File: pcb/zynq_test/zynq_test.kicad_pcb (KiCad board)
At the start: 2 copper layers, 100 x 100 mm, 19 parts, among them J1002 USB_A, J1101 RJ45_JK0654219, J1201 1-1734248-5, J1202 1-1734248-5, J1204 1-1734248-5, J702 USB_B_Micro, J801 HDMI_A, J802 HDMI_A, J901 A-MicroTF-1.85A, U1002 TUSB1210-Q1, U1003 AP22816AKBWT, U1102 LAN8830, U202 XC7Z020-2CLG400I, U401 MT41K256M16TW-107, U402 MT41K256M16TW-107, U702 FT2232HQ, U803 TDP1204RNQR, U806 TDP1204RNQR, U901 TXS02612RTW

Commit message: Finished Power Supply
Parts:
- moved J1204 23.1 mm to (175.0, 76.0), turned to 90 degrees
- moved J1201 20.3 mm to (152.0, 122.5), turned to -90 degrees
- moved J1002 16.4 mm to (124.5, 47.0)
- moved U1002 15.9 mm to (125.2, 61.5)
- moved J1202 14.2 mm to (159.7, 122.5), turned to 90 degrees
- moved U702 9.55 mm to (162.8, 61.5)
- moved J801 7.40 mm to (175.5, 118.7)
- moved J802 7.40 mm to (175.1, 99.2)
- moved U803 7.40 mm to (160.9, 97.2)
- moved U806 7.40 mm to (161.1, 117.6)
- moved U901 5.92 mm to (138.6, 68.8)
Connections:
- J1101 pad 14: +3.3V -> +3V3
- J1101 pad 16: +3.3V -> +3V3
- J1201 pad 10: unconnected-(J1201-Pad10) -> GND
- J1201 pad 10_1: unconnected-(J1201-10__1-Pad10_1) -> GND
- J1201 pad 11: unconnected-(J1201-Pad11) -> /Cameras/CAM0.GPIO0
- J1201 pad 11_1: unconnected-(J1201-11__1-Pad11_1) -> /Cameras/CAM0.GPIO0
- J1201 pad 12: unconnected-(J1201-Pad12) -> /Cameras/CAM0.GPIO1
- J1201 pad 12_1: unconnected-(J1201-12__1-Pad12_1) -> /Cameras/CAM0.GPIO1
- J1201 pad 13: unconnected-(J1201-Pad13) -> /Cameras/CAM_RX.0.I2C_CLK
- J1201 pad 13_1: unconnected-(J1201-13__1-Pad13_1) -> /Cameras/CAM_RX.0.I2C_CLK
- J1201 pad 14: unconnected-(J1201-Pad14) -> /Cameras/CAM_RX.0.I2C_SDA
- J1201 pad 14_1: unconnected-(J1201-14__1-Pad14_1) -> /Cameras/CAM_RX.0.I2C_SDA
- J1201 pad 15: unconnected-(J1201-Pad15) -> +3V3
- J1201 pad 15_1: unconnected-(J1201-15__1-Pad15_1) -> +3V3
- J1201 pad 1_1: /Cameras/CAM_RX.0.CAM_D0_N -> GND
- J1201 pad 2: /Cameras/CAM_RX.0.CAM_D0_P -> /Cameras/CAM_RX.0.CAM_D0_N
- J1201 pad 2_1: GND -> /Cameras/CAM_RX.0.CAM_D0_N
- J1201 pad 3: /Cameras/CAM_RX.0.CAM_D1_N -> /Cameras/CAM_RX.0.CAM_D0_P
- J1201 pad 3_1: /Cameras/CAM_RX.0.CAM_D1_P -> /Cameras/CAM_RX.0.CAM_D0_P
- J1201 pad 4_1: /Cameras/CAM_RX.0.CAM_CLK_N -> GND
- J1201 pad 5: /Cameras/CAM_RX.0.CAM_CLK_P -> /Cameras/CAM_RX.0.CAM_D1_N
- J1201 pad 5_1: GND -> /Cameras/CAM_RX.0.CAM_D1_N
- J1201 pad 6: /Cameras/CAM0.GPIO0 -> /Cameras/CAM_RX.0.CAM_D1_P
- J1201 pad 6_1: /Cameras/CAM0.GPIO1 -> /Cameras/CAM_RX.0.CAM_D1_P
- J1201 pad 7: /Cameras/CAM_RX.0.I2C_CLK -> GND
- J1201 pad 7_1: /Cameras/CAM_RX.0.I2C_SDA -> GND
- J1201 pad 8: +3.3V -> /Cameras/CAM_RX.0.CAM_CLK_N
- J1201 pad 8_1: unconnected-(J1201-8__1-Pad8_1) -> /Cameras/CAM_RX.0.CAM_CLK_N
- J1201 pad 9: unconnected-(J1201-Pad9) -> /Cameras/CAM_RX.0.CAM_CLK_P
- J1201 pad 9_1: unconnected-(J1201-9__1-Pad9_1) -> /Cameras/CAM_RX.0.CAM_CLK_P
- J1202 pad 10: unconnected-(J1202-Pad10) -> GND
- J1202 pad 10_1: unconnected-(J1202-10__1-Pad10_1) -> GND
- J1202 pad 11: unconnected-(J1202-Pad11) -> /Cameras/CAM1.GPIO0
- J1202 pad 11_1: unconnected-(J1202-11__1-Pad11_1) -> /Cameras/CAM1.GPIO0
- J1202 pad 12: unconnected-(J1202-Pad12) -> /Cameras/CAM1.GPIO1
- J1202 pad 12_1: unconnected-(J1202-12__1-Pad12_1) -> /Cameras/CAM1.GPIO1
- J1202 pad 13: unconnected-(J1202-Pad13) -> /Cameras/CAM_RX.1.I2C_CLK
- J1202 pad 13_1: unconnected-(J1202-13__1-Pad13_1) -> /Cameras/CAM_RX.1.I2C_CLK
- J1202 pad 14: unconnected-(J1202-Pad14) -> /Cameras/CAM_RX.1.I2C_SDA
- J1202 pad 14_1: unconnected-(J1202-14__1-Pad14_1) -> /Cameras/CAM_RX.1.I2C_SDA
- J1202 pad 15: unconnected-(J1202-Pad15) -> +3V3
- J1202 pad 15_1: unconnected-(J1202-15__1-Pad15_1) -> +3V3
- J1202 pad 1_1: /Cameras/CAM_RX.1.CAM_D0_N -> GND
- J1202 pad 2: /Cameras/CAM_RX.1.CAM_D0_P -> /Cameras/CAM_RX.1.CAM_D0_N
- J1202 pad 2_1: GND -> /Cameras/CAM_RX.1.CAM_D0_N
- J1202 pad 3: /Cameras/CAM_RX.1.CAM_D1_N -> /Cameras/CAM_RX.1.CAM_D0_P
- J1202 pad 3_1: /Cameras/CAM_RX.1.CAM_D1_P -> /Cameras/CAM_RX.1.CAM_D0_P
- J1202 pad 4_1: /Cameras/CAM_RX.1.CAM_CLK_N -> GND
- J1202 pad 5: /Cameras/CAM_RX.1.CAM_CLK_P -> /Cameras/CAM_RX.1.CAM_D1_N
- J1202 pad 5_1: GND -> /Cameras/CAM_RX.1.CAM_D1_N
- J1202 pad 6: /Cameras/CAM1.GPIO0 -> /Cameras/CAM_RX.1.CAM_D1_P
- J1202 pad 6_1: /Cameras/CAM1.GPIO1 -> /Cameras/CAM_RX.1.CAM_D1_P
- J1202 pad 7: /Cameras/CAM_RX.1.I2C_CLK -> GND
- J1202 pad 7_1: /Cameras/CAM_RX.1.I2C_SDA -> GND
- J1202 pad 8: +3.3V -> /Cameras/CAM_RX.1.CAM_CLK_N
- J1202 pad 8_1: unconnected-(J1202-8__1-Pad8_1) -> /Cameras/CAM_RX.1.CAM_CLK_N
- J1202 pad 9: unconnected-(J1202-Pad9) -> /Cameras/CAM_RX.1.CAM_CLK_P
- J1202 pad 9_1: unconnected-(J1202-9__1-Pad9_1) -> /Cameras/CAM_RX.1.CAM_CLK_P
- J1204 pad 10: unconnected-(J1204-Pad10) -> GND
- J1204 pad 10_1: unconnected-(J1204-10__1-Pad10_1) -> GND
- J1204 pad 11: unconnected-(J1204-Pad11) -> /Cameras/CAM2.GPIO0
- J1204 pad 11_1: unconnected-(J1204-11__1-Pad11_1) -> /Cameras/CAM2.GPIO0
- J1204 pad 12: unconnected-(J1204-Pad12) -> /Cameras/CAM2.GPIO1
- J1204 pad 12_1: unconnected-(J1204-12__1-Pad12_1) -> /Cameras/CAM2.GPIO1
- J1204 pad 13: unconnected-(J1204-Pad13) -> /Cameras/CAM_TX.2.I2C_CLK
- J1204 pad 13_1: unconnected-(J1204-13__1-Pad13_1) -> /Cameras/CAM_TX.2.I2C_CLK
- J1204 pad 14: unconnected-(J1204-Pad14) -> /Cameras/CAM_TX.2.I2C_SDA
- J1204 pad 14_1: unconnected-(J1204-14__1-Pad14_1) -> /Cameras/CAM_TX.2.I2C_SDA
- J1204 pad 15: unconnected-(J1204-Pad15) -> +3V3
- J1204 pad 15_1: unconnected-(J1204-15__1-Pad15_1) -> +3V3
- J1204 pad 1_1: /Cameras/CAM2.TX.0_N -> GND
- J1204 pad 2: /Cameras/CAM2.TX.0_P -> /Cameras/CAM2.TX.0_N
- J1204 pad 2_1: GND -> /Cameras/CAM2.TX.0_N
- J1204 pad 3: /Cameras/CAM2.TX.1_N -> /Cameras/CAM2.TX.0_P
- J1204 pad 3_1: /Cameras/CAM2.TX.1_P -> /Cameras/CAM2.TX.0_P
- J1204 pad 4_1: /Cameras/CAM2.TX.CLK_N -> GND
- J1204 pad 5: /Cameras/CAM2.TX.CLK_P -> /Cameras/CAM2.TX.1_N
- J1204 pad 5_1: GND -> /Cameras/CAM2.TX.1_N
- J1204 pad 6: /Cameras/CAM2.GPIO0 -> /Cameras/CAM2.TX.1_P
- J1204 pad 6_1: /Cameras/CAM2.GPIO1 -> /Cameras/CAM2.TX.1_P
- J1204 pad 7: /Cameras/CAM_TX.2.I2C_CLK -> GND
- J1204 pad 7_1: /Cameras/CAM_TX.2.I2C_SDA -> GND
- J1204 pad 8: +3.3V -> /Cameras/CAM2.TX.CLK_N
- J1204 pad 8_1: unconnected-(J1204-8__1-Pad8_1) -> /Cameras/CAM2.TX.CLK_N
- J1204 pad 9: unconnected-(J1204-Pad9) -> /Cameras/CAM2.TX.CLK_P
- J1204 pad 9_1: unconnected-(J1204-9__1-Pad9_1) -> /Cameras/CAM2.TX.CLK_P
- J901 pad 4: +3.3V -> +3V3
- U1002 pad 20: +3.3V -> +3V3
- U1002 pad 21: +3.3V -> +3V3
- U1003 pad 3: unconnected-(U1003-~{FLG}-Pad3) -> +5V
- U1003 pad 5: +5V -> +5V_{USB_OTG}
- U202 pad B6: +3.3V -> +3V3
- U202 pad C19: Net-(C302-Pad1) -> +3V3
- U202 pad D7: +3.3V -> +3V3
- U202 pad F18: Net-(C302-Pad1) -> +3V3
- U202 pad H14: Net-(C302-Pad1) -> +3V3
- U202 pad J17: Net-(C302-Pad1) -> +3V3
- U202 pad K20: Net-(C302-Pad1) -> +3V3
- U202 pad K6: +3.3V -> +3V3
- U202 pad M16: Net-(C302-Pad1) -> +3V3
- U202 pad M6: +3.3V -> +3V3
- U202 pad N19: Net-(C315-Pad1) -> +3V3
- U202 pad N6: +3.3V -> +3V3
- U202 pad R15: Net-(C315-Pad1) -> +3V3
- U202 pad R6: +3.3V -> +3V3
- U202 pad T18: Net-(C315-Pad1) -> +3V3
- U202 pad T6: +3.3V -> +3V3
- U202 pad T8: Net-(C301-Pad1) -> +3V3
- U202 pad U11: Net-(C301-Pad1) -> +3V3
- U202 pad V14: Net-(C315-Pad1) -> +3V3
- U202 pad W17: Net-(C315-Pad1) -> +3V3
- U202 pad W7: Net-(C301-Pad1) -> +3V3
- U202 pad Y10: Net-(C301-Pad1) -> +3V3
- U202 pad Y20: Net-(C315-Pad1) -> +3V3
- U702 pad 20: +3.3V -> +3V3
- U702 pad 31: +3.3V -> +3V3
- U702 pad 42: +3.3V -> +3V3
- U702 pad 50: +3.3V -> +3V3
- U702 pad 56: +3.3V -> +3V3
- U803 pad 1: +3.3V -> +3V3
- U803 pad 14: +3.3V -> +3V3
- U803 pad 20: +3.3V -> +3V3
- U803 pad 28: +3.3V -> +3V3
- U803 pad 6: +3.3V -> +3V3
- U803 pad 7: /HDMI/TX_EQ0 -> /HDMI/HDMI.EN
- U806 pad 1: +3.3V -> +3V3
- U806 pad 10: /HDMI/HDMI.RX.D2_N -> Net-(J801-D2-)
- U806 pad 11: Net-(J801-HPD) -> unconnected-(U806-HPD_OUT-Pad11)
- U806 pad 12: /HDMI/HDMI.RX.D1_P -> Net-(J801-D1+)
- U806 pad 13: /HDMI/HDMI.RX.D1_N -> Net-(J801-D1-)
- U806 pad 14: +3.3V -> +3V3
- U806 pad 15: /HDMI/HDMI.RX.D0_P -> Net-(J801-D0+)
- U806 pad 16: /HDMI/HDMI.RX.D0_N -> Net-(J801-D0-)
- U806 pad 18: /HDMI/HDMI.RX.CLK_P -> Net-(J801-CK+)
- U806 pad 19: /HDMI/HDMI.RX.CLK_N -> Net-(J801-CK-)
- U806 pad 20: +3.3V -> +3V3
- U806 pad 28: +3.3V -> +3V3
- U806 pad 30: Net-(J801-CK-) -> /HDMI/HDMI.RX.CLK_N
- U806 pad 31: Net-(J801-CK+) -> /HDMI/HDMI.RX.CLK_P
- U806 pad 32: unconnected-(U806-HPD_IN-Pad32) -> Net-(J801-HPD)
- U806 pad 33: Net-(J801-D0-) -> /HDMI/HDMI.RX.D0_N
- U806 pad 34: Net-(J801-D0+) -> /HDMI/HDMI.RX.D0_P
- U806 pad 36: Net-(J801-D1-) -> /HDMI/HDMI.RX.D1_N
- U806 pad 37: Net-(J801-D1+) -> /HDMI/HDMI.RX.D1_P
- U806 pad 39: Net-(J801-D2-) -> /HDMI/HDMI.RX.D2_N
- U806 pad 40: Net-(J801-D2+) -> /HDMI/HDMI.RX.D2_P
- U806 pad 6: +3.3V -> +3V3
- U806 pad 7: /HDMI/RX_EQ0 -> /HDMI/HDMI.EN
- U806 pad 9: /HDMI/HDMI.RX.D2_P -> Net-(J801-D2+)
- U901 pad 17: +3.3V -> +3V3
- U901 pad 21: +3.3V -> +3V3
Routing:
- net /USB_OTG/USB_OTG.D-: track 0.00 -> 0.88 mm

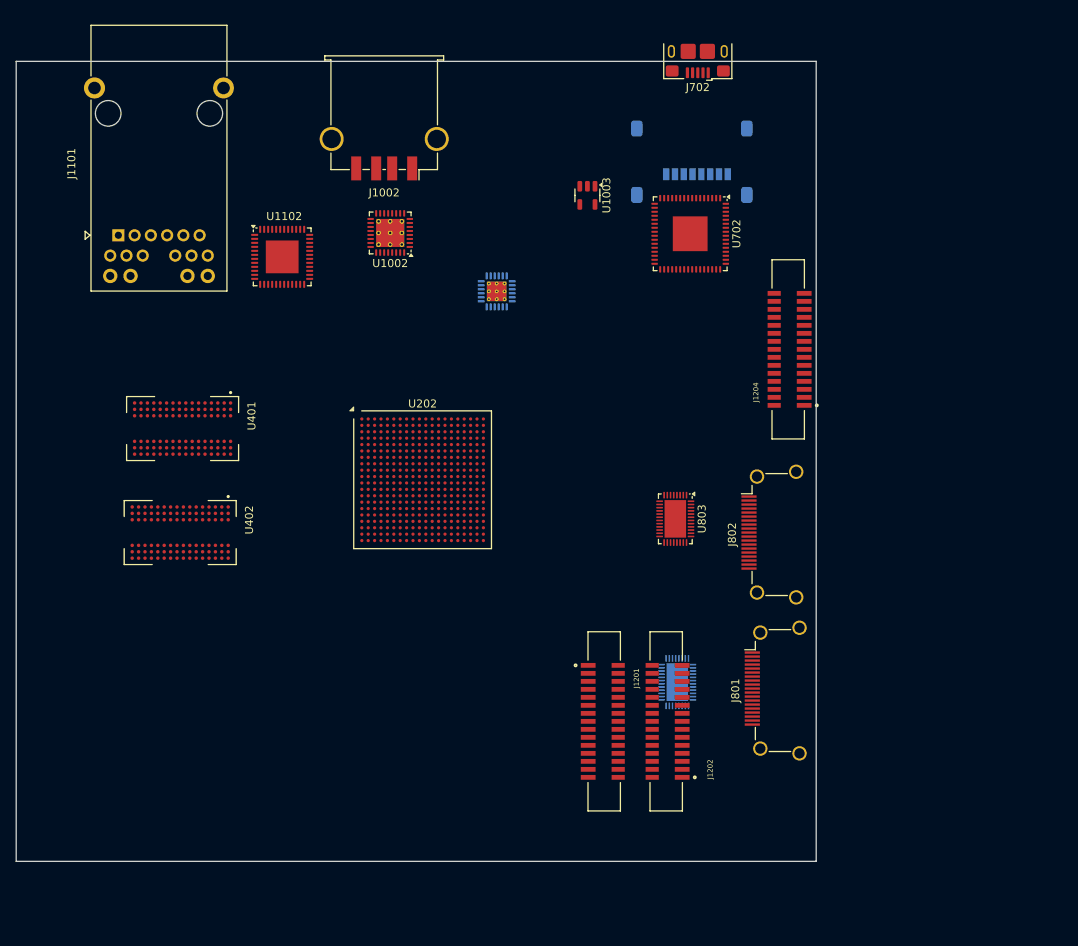
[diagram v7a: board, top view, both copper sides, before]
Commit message: Finished most of the schematic, will start routing soon
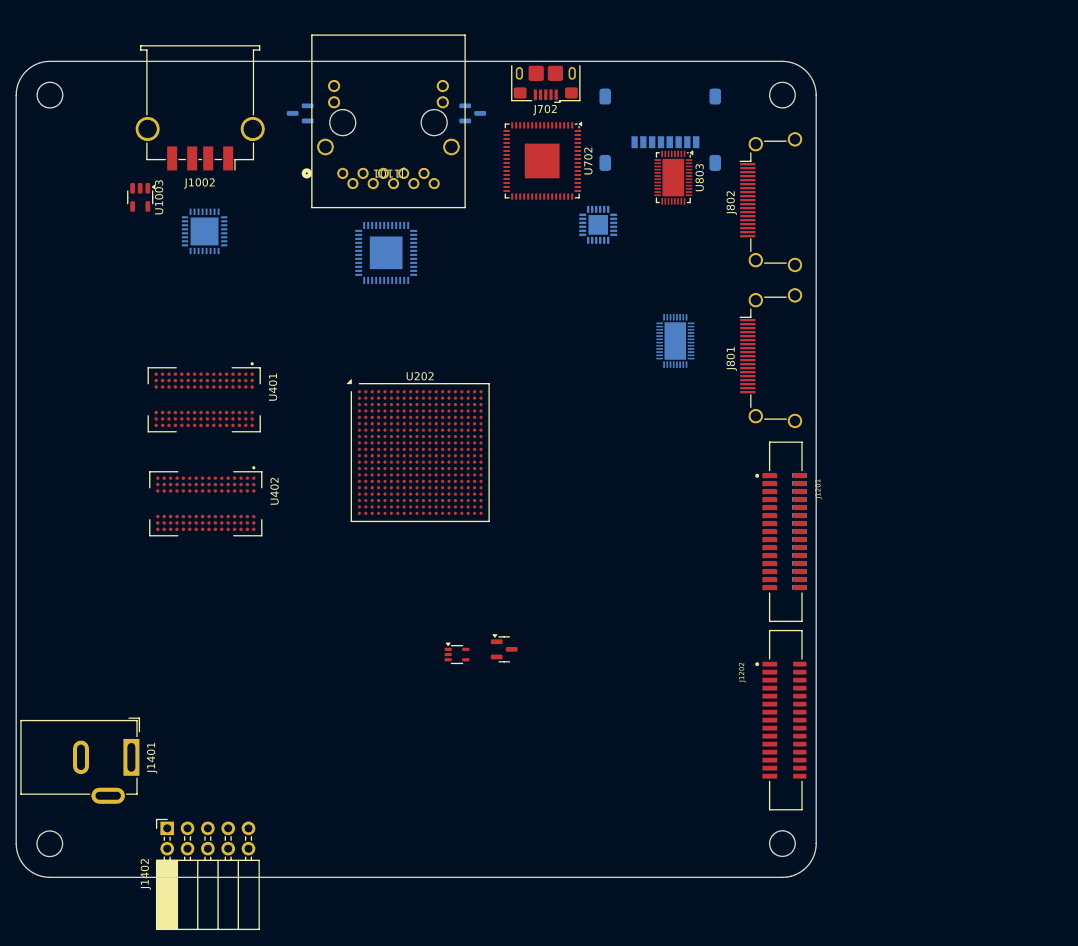
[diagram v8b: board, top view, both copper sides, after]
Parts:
- added J1401: Barrel_Jack, Connector_BarrelJack:BarrelJack_GCT_DCJ200-10-A_Horizontal, F.Cu at (92.9, 127.0)
- added J1402: Conn_02x05_Odd_Even, Connector_PinSocket_2.54mm:PinSocket_2x05_P2.54mm_Horizontal, F.Cu at (97.4, 135.9)
- added Q1102: 2N7002E, Package_TO_SOT_SMD:SOT-23, B.Cu at (135.6, 46.5)
- added Q1103: 2N7002E, Package_TO_SOT_SMD:SOT-23, B.Cu at (114.0, 46.5)
- added Q1104: 2N7002E, Package_TO_SOT_SMD:SOT-23, F.Cu at (139.5, 113.5)
- added U1405: 74LVC1G17, Package_TO_SOT_SMD:Texas_R-PDSO-G5_DCK-5, F.Cu at (133.6, 114.2)
- J1101: footprint Connector_RJ:RJ45_Pulse_JK0654219NL_Horizontal -> ethernet:ARJM11C7-502-AB-ER2-T_ABR
- J1204, U1102: moved to B.Cu
- U1002: footprint Package_DFN_QFN:VQFN-32-1EP_5x5mm_P0.5mm_EP3.5x3.5mm_ThermalVias -> Package_DFN_QFN:VQFN-32-1EP_5x5mm_P0.5mm_EP3.5x3.5mm; moved to B.Cu
- U901: footprint Package_DFN_QFN:WQFN-24-1EP_4x4mm_P0.5mm_EP2.45x2.45mm_ThermalVias -> Package_DFN_QFN:WQFN-24-1EP_4x4mm_P0.5mm_EP2.45x2.45mm
- moved U1003 55.9 mm to (94.0, 57.0)
- moved U803 42.7 mm to (160.6, 54.5)
- moved U806 42.7 mm to (160.9, 75.0)
- moved J801 41.6 mm to (174.9, 77.1)
- moved J802 41.6 mm to (174.9, 57.6)
- moved J1201 32.8 mm to (174.7, 98.8)
- moved J1101 29.1 mm to (119.3, 54.0), turned to 180 degrees
- moved U1002 23.2 mm to (102.0, 61.2), turned to 90 degrees
- moved J1002 23.0 mm to (101.5, 45.8)
- moved J1204 22.8 mm to (174.4, 98.8), turned to -90 degrees
- moved U702 20.6 mm to (144.2, 52.5)
- moved J702 19.2 mm to (144.7, 41.5)
- moved U901 15.2 mm to (151.2, 60.4)
- moved J1202 15.0 mm to (174.7, 122.3), turned to -90 degrees
- moved U1102 13.0 mm to (124.8, 63.9), turned to -90 degrees
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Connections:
- net /Zynq Mio/MIO0.0 renamed /GPIO/MIO0.0
- net /Zynq Mio/MIO0.10 renamed /GPIO/MIO0.10
- net /Zynq Mio/MIO0.11 renamed /GPIO/MIO0.11
- net /Zynq Mio/MIO0.12 renamed /GPIO/MIO0.12
- net /Zynq Mio/MIO0.13 renamed /GPIO/MIO0.13
- net /Zynq Mio/MIO0.7 renamed /GPIO/MIO0.7
- net /Zynq Mio/MIO0.8 renamed /GPIO/MIO0.8
- net /Zynq Mio/MIO0.9 renamed /GPIO/MIO0.9
- net /Zynq Mio/MIO1.46 renamed /GPIO/MIO1.46
- net /Zynq Mio/MIO1.47 renamed /GPIO/MIO1.47
- net /Zynq Mio/MIO1.48 renamed /GPIO/MIO1.48
- net /Zynq Mio/MIO1.49 renamed /GPIO/MIO1.49
- net /Zynq Mio/MIO1.50 renamed /GPIO/MIO1.50
- net /Zynq Mio/MIO1.51 renamed /GPIO/MIO1.51
- J1101 pad 1: /ETHERNET/ETH_TX3_C -> /ETHERNET/ETH_TX1_P
- J1101 pad 10: /ETHERNET/ETH_TX1_N -> /ETHERNET/ETH_TX4_N
- J1101 pad 11: /ETHERNET/ETH_TX1_P -> +3V3
- J1101 pad 12: /ETHERNET/ETH_TX1_C -> /ETHERNET/LED1
- J1101 pad 13: /ETHERNET/LED2 -> +3V3
- J1101 pad 14: +3V3 -> /ETHERNET/LED2
- J1101 pad 2: /ETHERNET/ETH_TX3_N -> /ETHERNET/ETH_TX1_N
- J1101 pad 3: /ETHERNET/ETH_TX3_P -> /ETHERNET/ETH_TX2_P
- J1101 pad 4: /ETHERNET/ETH_TX2_P -> /ETHERNET/ETH_TX2_N
- J1101 pad 5: /ETHERNET/ETH_TX2_N -> Net-(J1101-TRCT1)
- J1101 pad 6: /ETHERNET/ETH_TX2_C -> Net-(J1101-TRCT1)
- J1101 pad 7: /ETHERNET/ETH_TX4_C -> /ETHERNET/ETH_TX3_P
- J1101 pad 8: /ETHERNET/ETH_TX4_P -> /ETHERNET/ETH_TX3_N
- J1101 pad 9: /ETHERNET/ETH_TX4_N -> /ETHERNET/ETH_TX4_P
- J1201 pad 11: /Cameras/CAM0.GPIO0 -> /Cameras/CAM0.GPIO1.
- J1201 pad 11_1: /Cameras/CAM0.GPIO0 -> /Cameras/CAM0.GPIO1.
- J1201 pad 12: /Cameras/CAM0.GPIO1 -> /Cameras/CAM0.GPIO1.
- J1201 pad 12_1: /Cameras/CAM0.GPIO1 -> /Cameras/CAM0.GPIO1.
- J1202 pad 11: /Cameras/CAM1.GPIO0 -> /Cameras/CAM1.GPIO1.
- J1202 pad 11_1: /Cameras/CAM1.GPIO0 -> /Cameras/CAM1.GPIO1.
- J1202 pad 12: /Cameras/CAM1.GPIO1 -> /Cameras/CAM1.GPIO1.
- J1202 pad 12_1: /Cameras/CAM1.GPIO1 -> /Cameras/CAM1.GPIO1.
- J1204 pad 11: /Cameras/CAM2.GPIO0 -> /Cameras/CAM2.GPIO1.
- J1204 pad 11_1: /Cameras/CAM2.GPIO0 -> /Cameras/CAM2.GPIO1.
- J1204 pad 12: /Cameras/CAM2.GPIO1 -> /Cameras/CAM2.GPIO1.
- J1204 pad 12_1: /Cameras/CAM2.GPIO1 -> /Cameras/CAM2.GPIO1.
- U1102 pad 42: /ETHERNET/CLK_125M -> /Zynq FPGA/CLK_125M
- U202 pad A20: unconnected-(U202D-IO_L2N_T0_AD8N_35-PadA20) -> /HDMI/HDMI.TX.D2_N
- U202 pad B19: unconnected-(U202D-IO_L2P_T0_AD8P_35-PadB19) -> /HDMI/HDMI.TX.D2_P
- U202 pad B20: unconnected-(U202D-IO_L1N_T0_AD0N_35-PadB20) -> /HDMI/HDMI.TX.D1_N
- U202 pad C20: unconnected-(U202D-IO_L1P_T0_AD0P_35-PadC20) -> /HDMI/HDMI.TX.D1_P
- U202 pad C7: /Zynq PWR+JTAG/PWR_ON_RST -> /Power/PWR_ON_RST
- U202 pad D18: unconnected-(U202D-IO_L3N_T0_DQS_AD1N_35-PadD18) -> /HDMI/HDMI.RX.D2_N
- U202 pad D19: unconnected-(U202D-IO_L4P_T0_35-PadD19) -> /HDMI/HDMI.TX.D0_P
- U202 pad D20: unconnected-(U202D-IO_L4N_T0_35-PadD20) -> /HDMI/HDMI.TX.D0_N
- U202 pad E17: unconnected-(U202D-IO_L3P_T0_DQS_AD1P_35-PadE17) -> /HDMI/HDMI.RX.D2_P
- U202 pad E18: unconnected-(U202D-IO_L5P_T0_AD9P_35-PadE18) -> /HDMI/HDMI.TX.CLK_P
- U202 pad E19: unconnected-(U202D-IO_L5N_T0_AD9N_35-PadE19) -> /HDMI/HDMI.TX.CLK_N
- U202 pad F16: unconnected-(U202D-IO_L6P_T0_35-PadF16) -> /HDMI/HDMI.RX.D1_P
- U202 pad F17: unconnected-(U202D-IO_L6N_T0_VREF_35-PadF17) -> /HDMI/HDMI.RX.D1_N
- U202 pad F19: unconnected-(U202D-IO_L15P_T2_DQS_AD12P_35-PadF19) -> /Cameras/CAM_RX.0.CAM_D0_P
- U202 pad F20: unconnected-(U202D-IO_L15N_T2_DQS_AD12N_35-PadF20) -> /Cameras/CAM_RX.0.CAM_D0_N
- U202 pad G14: unconnected-(U202D-IO_0_35-PadG14) -> /HDMI/HDMI.TX.SCL
- U202 pad G15: unconnected-(U202D-IO_L19N_T3_VREF_35-PadG15) -> /HDMI/HDMI.RX.D0_N
- U202 pad G17: unconnected-(U202D-IO_L16P_T2_35-PadG17) -> /HDMI/HDMI.RX.CLK_P
- U202 pad G18: unconnected-(U202D-IO_L16N_T2_35-PadG18) -> /HDMI/HDMI.RX.CLK_N
- U202 pad G19: unconnected-(U202D-IO_L18P_T2_AD13P_35-PadG19) -> /Cameras/CAM_RX.0.LN_0_P
- U202 pad G20: unconnected-(U202D-IO_L18N_T2_AD13N_35-PadG20) -> /Cameras/CAM_RX.0.LN_0_N
- U202 pad H15: unconnected-(U202D-IO_L19P_T3_35-PadH15) -> /HDMI/HDMI.RX.D0_P
- U202 pad H16: unconnected-(U202D-IO_L13P_T2_MRCC_35-PadH16) -> /Zynq FPGA/CLK_125M
- U202 pad H18: unconnected-(U202D-IO_L14N_T2_AD4N_SRCC_35-PadH18) -> /HDMI/HDMI.RX.SDA
- U202 pad H20: unconnected-(U202D-IO_L17N_T2_AD5N_35-PadH20) -> /Cameras/CAM_RX.0.CAM_D1_N
- U202 pad J14: unconnected-(U202D-IO_L20N_T3_AD6N_35-PadJ14) -> /HDMI/HDMI.TX.HDP
- U202 pad J15: unconnected-(U202D-IO_25_35-PadJ15) -> /HDMI/HDMI.TX.SDA
- U202 pad J16: unconnected-(U202D-IO_L24N_T3_AD15N_35-PadJ16) -> /HDMI/HDMI.CTR.SCL
- U202 pad J18: unconnected-(U202D-IO_L14P_T2_AD4P_SRCC_35-PadJ18) -> /HDMI/HDMI.RX.SCL
- U202 pad J19: unconnected-(U202D-IO_L10N_T1_AD11N_35-PadJ19) -> /Cameras/CAM_RX.0.LN_1_N
- U202 pad J20: unconnected-(U202D-IO_L17P_T2_AD5P_35-PadJ20) -> /Cameras/CAM_RX.0.CAM_D1_P
- U202 pad K14: unconnected-(U202D-IO_L20P_T3_AD6P_35-PadK14) -> /ETHERNET/ETH0_INT
- U202 pad K16: unconnected-(U202D-IO_L24P_T3_AD15P_35-PadK16) -> /HDMI/HDMI.CTR.SDA
- U202 pad K17: unconnected-(U202D-IO_L12P_T1_MRCC_35-PadK17) -> /Cameras/CAM_RX.0.I2C_CLK
- U202 pad K18: unconnected-(U202D-IO_L12N_T1_MRCC_35-PadK18) -> /Cameras/CAM_RX.0.I2C_SDA
- U202 pad K19: unconnected-(U202D-IO_L10P_T1_AD11P_35-PadK19) -> /Cameras/CAM_RX.0.LN_1_P
- U202 pad L14: unconnected-(U202D-IO_L22P_T3_AD7P_35-PadL14) -> /Zynq FPGA/ETH0_RST
- U202 pad L16: unconnected-(U202D-IO_L11P_T1_SRCC_35-PadL16) -> /HDMI/HDMI.EN
- U202 pad L19: unconnected-(U202D-IO_L9P_T1_DQS_AD3P_35-PadL19) -> /Cameras/CAM_RX.0.CAM_CLK_P
- U202 pad L20: unconnected-(U202D-IO_L9N_T1_DQS_AD3N_35-PadL20) -> /Cameras/CAM_RX.0.CAM_CLK_N
- U202 pad M19: unconnected-(U202D-IO_L7P_T1_AD2P_35-PadM19) -> /Cameras/CAM_RX.0.LN_CLK_P
- U202 pad M20: unconnected-(U202D-IO_L7N_T1_AD2N_35-PadM20) -> /Cameras/CAM_RX.0.LN_CLK_N
- U202 pad N17: unconnected-(U202C-IO_L23P_T3_34-PadN17) -> /GPIO/GPIO2.8
- U202 pad N18: unconnected-(U202C-IO_L13P_T2_MRCC_34-PadN18) -> /GPIO/GPIO2.2
- U202 pad N20: unconnected-(U202C-IO_L14P_T2_SRCC_34-PadN20) -> /GPIO/GPIO2.4
- U202 pad P14: unconnected-(U202C-IO_L6P_T0_34-PadP14) -> /GPIO/GPIO1.8
- U202 pad P15: unconnected-(U202C-IO_L24P_T3_34-PadP15) -> /Cameras/CAM_TX.2.LN_0_P
- U202 pad P16: unconnected-(U202C-IO_L24N_T3_34-PadP16) -> /Cameras/CAM_TX.2.LN_0_N
- U202 pad P18: unconnected-(U202C-IO_L23N_T3_34-PadP18) -> /GPIO/GPIO2.9
- U202 pad P19: unconnected-(U202C-IO_L13N_T2_MRCC_34-PadP19) -> /GPIO/GPIO2.3
- U202 pad P20: unconnected-(U202C-IO_L14N_T2_SRCC_34-PadP20) -> /GPIO/GPIO2.5
- U202 pad R14: unconnected-(U202C-IO_L6N_T0_VREF_34-PadR14) -> /GPIO/GPIO1.9
- U202 pad R16: unconnected-(U202C-IO_L19P_T3_34-PadR16) -> /Cameras/CAM_TX.2.CAM_D0_P
- U202 pad R17: unconnected-(U202C-IO_L19N_T3_VREF_34-PadR17) -> /Cameras/CAM_TX.2.CAM_D0_N
- U202 pad R18: unconnected-(U202C-IO_L20N_T3_34-PadR18) -> /Cameras/CAM_TX.2.LN_1_N
- U202 pad R19: unconnected-(U202C-IO_0_34-PadR19) -> /GPIO/GPIO2.0
- U202 pad T10: unconnected-(U202C-IO_L1N_T0_34-PadT10) -> /GPIO/GPIO1.1
- U202 pad T11: unconnected-(U202C-IO_L1P_T0_34-PadT11) -> /GPIO/GPIO1.0
- U202 pad T12: unconnected-(U202C-IO_L2P_T0_34-PadT12) -> /GPIO/GPIO1.2
- U202 pad T14: unconnected-(U202C-IO_L5P_T0_34-PadT14) -> /Cameras/CAM_TX.2.I2C_CLK
- U202 pad T15: unconnected-(U202C-IO_L5N_T0_34-PadT15) -> /Cameras/CAM_TX.2.I2C_SDA
- U202 pad T16: unconnected-(U202C-IO_L9P_T1_DQS_34-PadT16) -> /Cameras/CAM_TX.2.LN_CLK_P
- U202 pad T17: unconnected-(U202C-IO_L20P_T3_34-PadT17) -> /Cameras/CAM_TX.2.LN_1_P
- U202 pad T19: unconnected-(U202C-IO_25_34-PadT19) -> /GPIO/GPIO2.1
- U202 pad T20: unconnected-(U202C-IO_L15P_T2_DQS_34-PadT20) -> /GPIO/GPIO2.6
- U202 pad T5: unconnected-(U202B-IO_L19P_T3_13-PadT5) -> /GPIO/GPIO0.17
- U202 pad T8: +3V3 -> +1V8
- U202 pad T9: unconnected-(U202B-IO_L12P_T1_MRCC_13-PadT9) -> /GPIO/GPIO0.4
- U202 pad U10: unconnected-(U202B-IO_L12N_T1_MRCC_13-PadU10) -> /GPIO/GPIO0.3
- U202 pad U11: +3V3 -> +1V8
- U202 pad U12: unconnected-(U202C-IO_L2N_T0_34-PadU12) -> /GPIO/GPIO1.3
- U202 pad U13: unconnected-(U202C-IO_L3P_T0_DQS_PUDC_B_34-PadU13) -> /GPIO/GPIO1.4
- U202 pad U14: unconnected-(U202C-IO_L11P_T1_SRCC_34-PadU14) -> /GPIO/GPIO1.10
- U202 pad U15: unconnected-(U202C-IO_L11N_T1_SRCC_34-PadU15) -> /GPIO/GPIO1.11
- U202 pad U17: unconnected-(U202C-IO_L9N_T1_DQS_34-PadU17) -> /Cameras/CAM_TX.2.LN_CLK_N
- U202 pad U18: unconnected-(U202C-IO_L12P_T1_MRCC_34-PadU18) -> /Cameras/CAM_TX.2.CAM_D1_P
- U202 pad U19: unconnected-(U202C-IO_L12N_T1_MRCC_34-PadU19) -> /Cameras/CAM_TX.2.CAM_D1_N
- U202 pad U20: unconnected-(U202C-IO_L15N_T2_DQS_34-PadU20) -> /GPIO/GPIO2.7
- U202 pad U5: unconnected-(U202B-IO_L19N_T3_VREF_13-PadU5) -> /GPIO/GPIO0.18
- U202 pad U7: unconnected-(U202B-IO_L11P_T1_SRCC_13-PadU7) -> /GPIO/GPIO0.2
- U202 pad U8: unconnected-(U202B-IO_L17N_T2_13-PadU8) -> /GPIO/GPIO0.14
- U202 pad U9: unconnected-(U202B-IO_L17P_T2_13-PadU9) -> /GPIO/GPIO0.13
- U202 pad V10: unconnected-(U202B-IO_L21N_T3_DQS_13-PadV10) -> /GPIO/GPIO0.22
- U202 pad V11: unconnected-(U202B-IO_L21P_T3_DQS_13-PadV11) -> /GPIO/GPIO0.21
- U202 pad V12: unconnected-(U202C-IO_L4P_T0_34-PadV12) -> /GPIO/GPIO1.6
- U202 pad V13: unconnected-(U202C-IO_L3N_T0_DQS_34-PadV13) -> /GPIO/GPIO1.5
- U202 pad V15: unconnected-(U202C-IO_L10P_T1_34-PadV15) -> /Cameras/CAM_RX.1.CAM_CLK_P
- U202 pad V16: unconnected-(U202C-IO_L18P_T2_34-PadV16) -> /Cameras/CAM_RX.1.LN_1_P
- U202 pad V17: unconnected-(U202C-IO_L21P_T3_DQS_34-PadV17) -> /Cameras/CAM_TX.2.CAM_CLK_P
- U202 pad V18: unconnected-(U202C-IO_L21N_T3_DQS_34-PadV18) -> /Cameras/CAM_TX.2.CAM_CLK_N
- U202 pad V20: unconnected-(U202C-IO_L16P_T2_34-PadV20) -> /Cameras/CAM_RX.1.I2C_CLK
- U202 pad V5: unconnected-(U202B-IO_L6N_T0_VREF_13-PadV5) -> /GPIO/GPIO0.0
- U202 pad V6: unconnected-(U202B-IO_L22P_T3_13-PadV6) -> /GPIO/GPIO0.23
- U202 pad V7: unconnected-(U202B-IO_L11N_T1_SRCC_13-PadV7) -> /GPIO/GPIO0.1
- U202 pad V8: unconnected-(U202B-IO_L15P_T2_DQS_13-PadV8) -> /GPIO/GPIO0.10
- U202 pad W10: unconnected-(U202B-IO_L16P_T2_13-PadW10) -> /GPIO/GPIO0.11
- U202 pad W11: unconnected-(U202B-IO_L18P_T2_13-PadW11) -> /GPIO/GPIO0.15
- U202 pad W13: unconnected-(U202C-IO_L4N_T0_34-PadW13) -> /GPIO/GPIO1.7
- U202 pad W14: unconnected-(U202C-IO_L8P_T1_34-PadW14) -> /Cameras/CAM_RX.1.LN_CLK_P
- U202 pad W15: unconnected-(U202C-IO_L10N_T1_34-PadW15) -> /Cameras/CAM_RX.1.CAM_CLK_N
- U202 pad W16: unconnected-(U202C-IO_L18N_T2_34-PadW16) -> /Cameras/CAM_RX.1.LN_1_N
- U202 pad W18: unconnected-(U202C-IO_L22P_T3_34-PadW18) -> /Cameras/CAM_RX.1.LN_0_P
- U202 pad W19: unconnected-(U202C-IO_L22N_T3_34-PadW19) -> /Cameras/CAM_RX.1.LN_0_N
- U202 pad W20: unconnected-(U202C-IO_L16N_T2_34-PadW20) -> /Cameras/CAM_RX.1.I2C_SDA
- U202 pad W6: unconnected-(U202B-IO_L22N_T3_13-PadW6) -> /GPIO/GPIO0.24
- U202 pad W7: +3V3 -> +1V8
- U202 pad W8: unconnected-(U202B-IO_L15N_T2_DQS_13-PadW8) -> /GPIO/GPIO0.9
- U202 pad W9: unconnected-(U202B-IO_L16N_T2_13-PadW9) -> /GPIO/GPIO0.12
- U202 pad Y10: +3V3 -> +1V8
- U202 pad Y11: unconnected-(U202B-IO_L18N_T2_13-PadY11) -> /GPIO/GPIO0.16
- U202 pad Y12: unconnected-(U202B-IO_L20P_T3_13-PadY12) -> /GPIO/GPIO0.19
- U202 pad Y13: unconnected-(U202B-IO_L20N_T3_13-PadY13) -> /GPIO/GPIO0.20
- U202 pad Y14: unconnected-(U202C-IO_L8N_T1_34-PadY14) -> /Cameras/CAM_RX.1.LN_CLK_N
- U202 pad Y16: unconnected-(U202C-IO_L7P_T1_34-PadY16) -> /Cameras/CAM_RX.1.CAM_D1_P
- U202 pad Y17: unconnected-(U202C-IO_L7N_T1_34-PadY17) -> /Cameras/CAM_RX.1.CAM_D1_N
- U202 pad Y18: unconnected-(U202C-IO_L17P_T2_34-PadY18) -> /Cameras/CAM_RX.1.CAM_D0_P
- U202 pad Y19: unconnected-(U202C-IO_L17N_T2_34-PadY19) -> /Cameras/CAM_RX.1.CAM_D0_N
- U202 pad Y6: unconnected-(U202B-IO_L13N_T2_MRCC_13-PadY6) -> /GPIO/GPIO0.5
- U202 pad Y7: unconnected-(U202B-IO_L13P_T2_MRCC_13-PadY7) -> /GPIO/GPIO0.6
- U202 pad Y8: unconnected-(U202B-IO_L14N_T2_SRCC_13-PadY8) -> /GPIO/GPIO0.7
- U202 pad Y9: unconnected-(U202B-IO_L14P_T2_SRCC_13-PadY9) -> /GPIO/GPIO0.8
- U702 pad 7: /Programmer/FTDI_D+ -> /Programmer/FTDI_D-
- U702 pad 8: /Programmer/FTDI_D- -> /Programmer/FTDI_D+
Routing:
- net /USB_OTG/USB_OTG.D-: track 0.88 -> 0.00 mm
- added copper zone on In1.Cu, net GND
- added copper zone on In4.Cu, net GND
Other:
- board size 100 x 100 mm -> 100 x 102 mm
- copper layers 2 -> 6
